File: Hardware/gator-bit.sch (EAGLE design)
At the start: 89 parts, among them J1 GATOR, J10 GATOR, J11 GATOR, J12 GATOR, J13 GATOR, J14 GATOR, J15 GATOR, J16 GATOR, J17 GATOR, J18 GATOR, J2 GATOR, J3 GATOR, J4 GATOR, J6 GATOR, J7 GATOR, J8 GATOR, J9 GATOR, U1 TPS63070, U2 micro:bit, U3 MIC52053.0V, U4 ADJ REG 1.5A

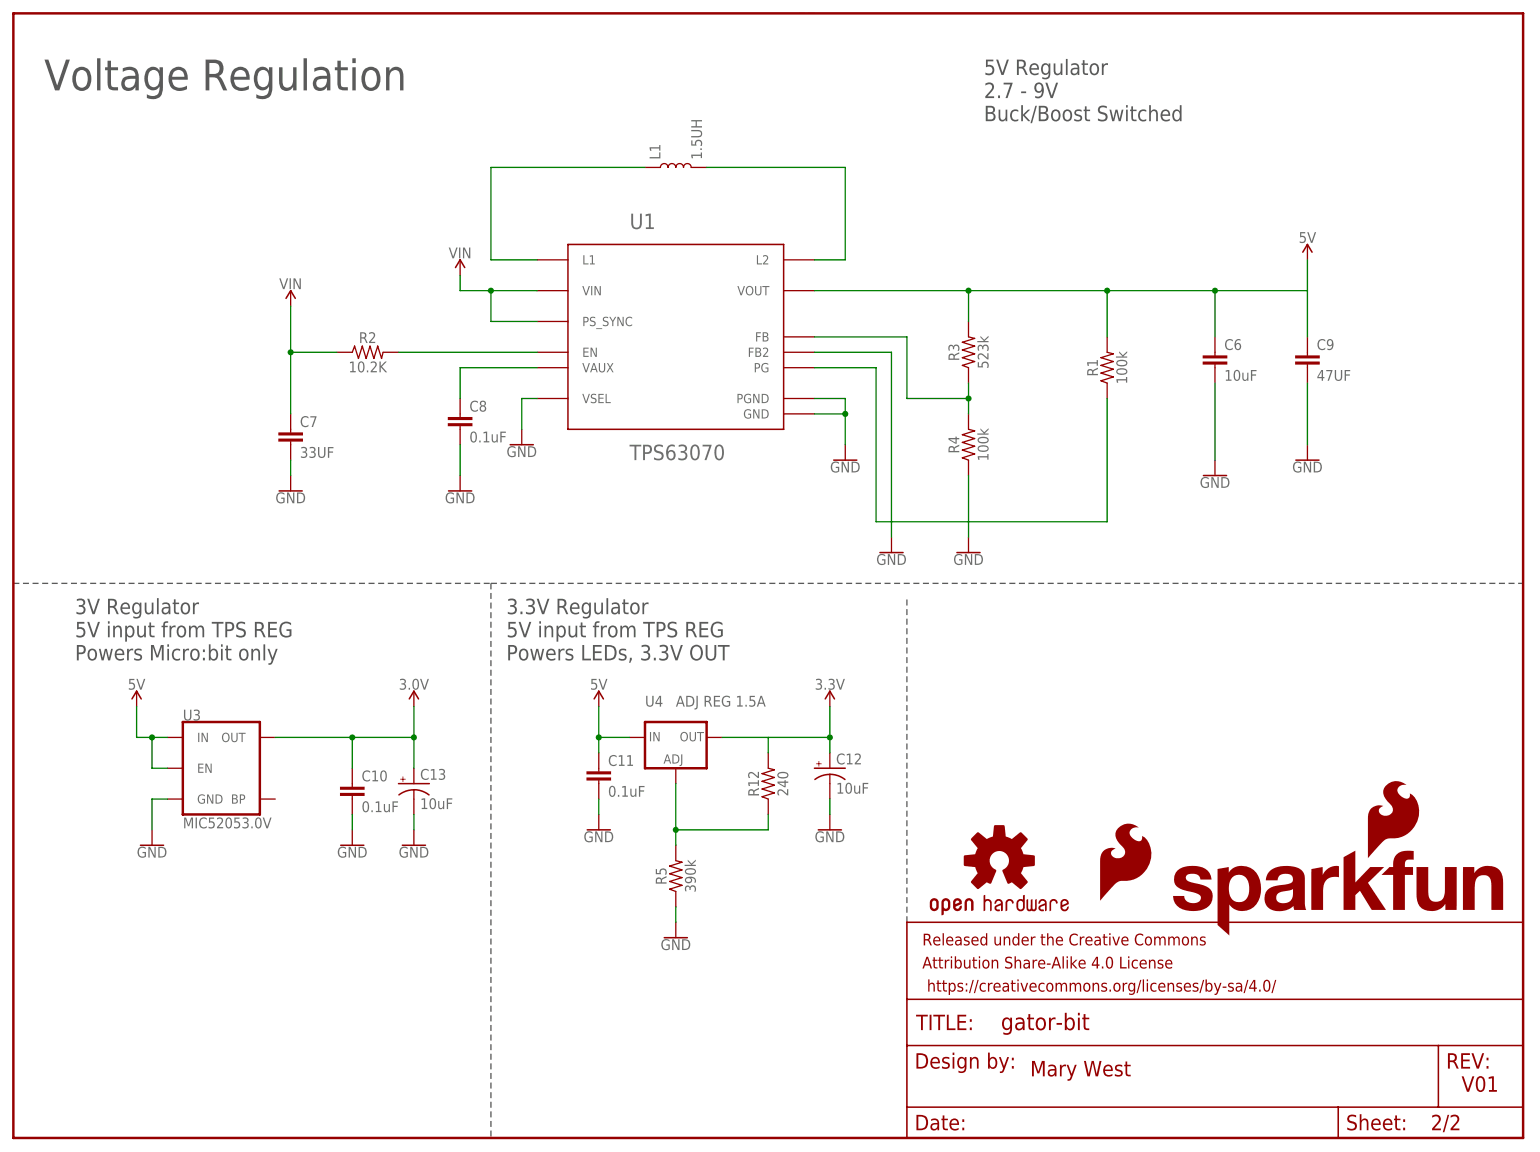
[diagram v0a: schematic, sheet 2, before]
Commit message: -Updated protection diodes -added a power path to be powered from the micro:bit -added master switch -added status LEDs
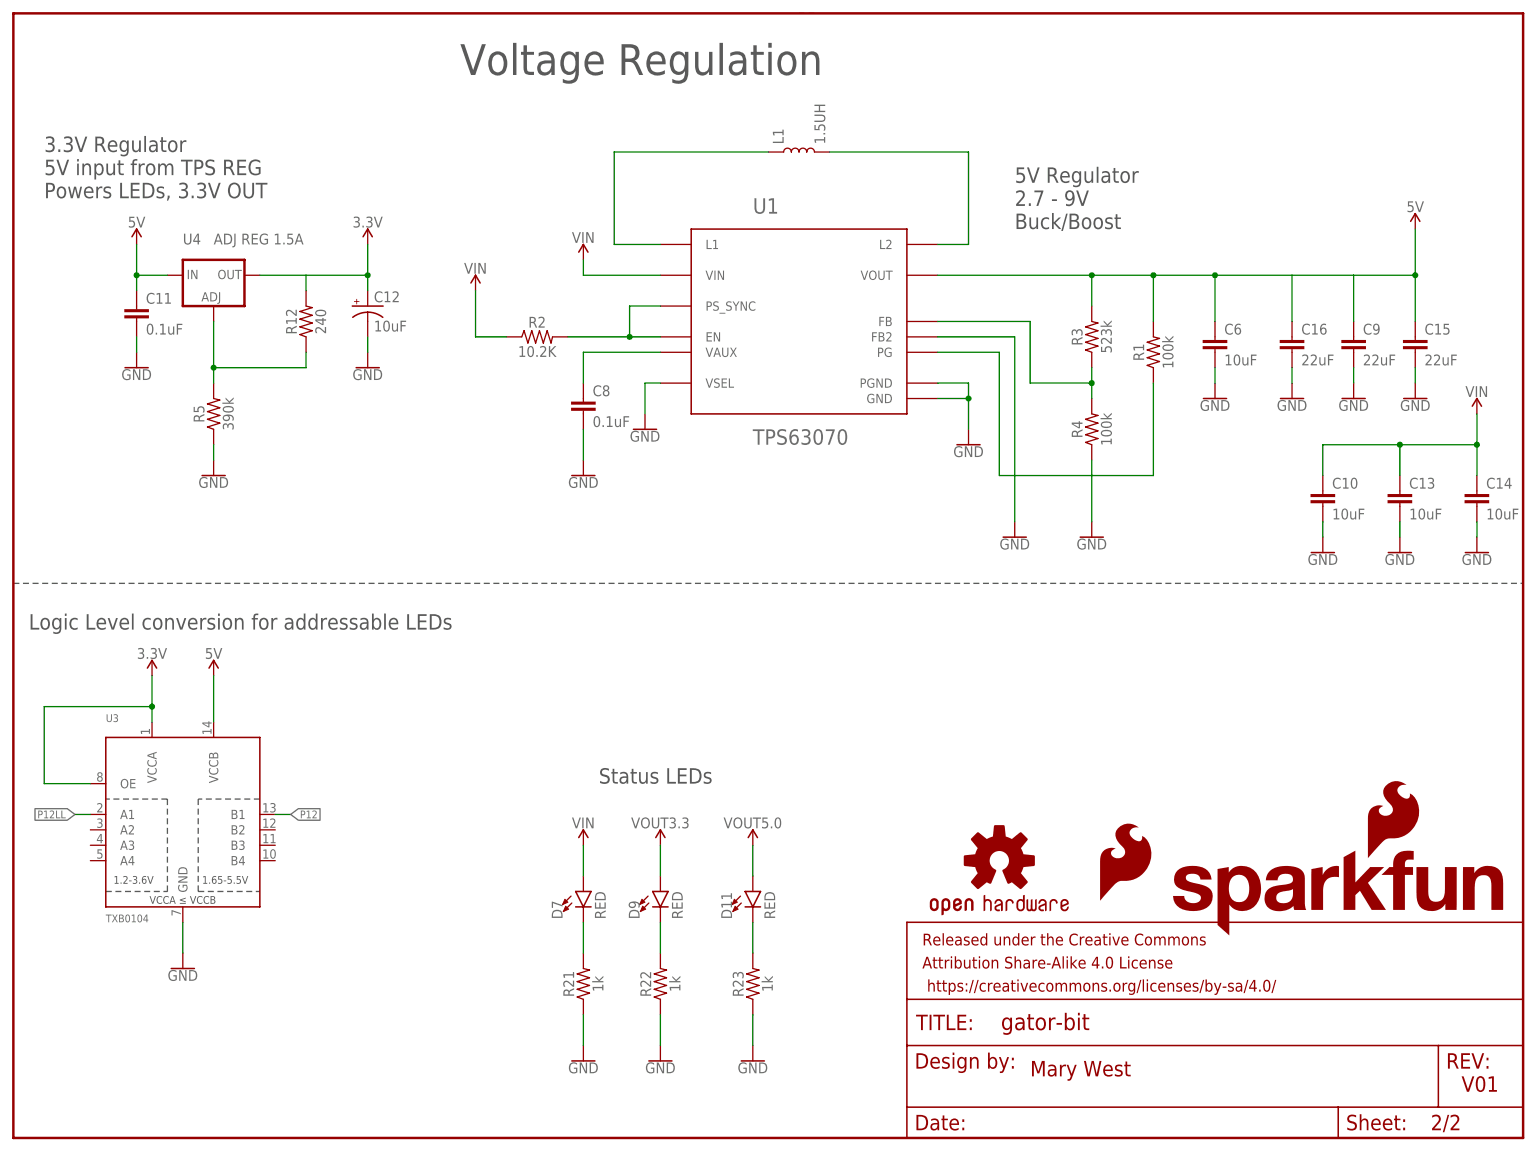
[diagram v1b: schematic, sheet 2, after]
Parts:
- removed C7: 33UF, SparkFun-Capacitors:33UF20%-6.3V-0805
- removed D14, D16, D18, D20: 3.3V, SparkFun-DiscreteSemi:DIODE-ZENER-MM3Z3V3T1G
- added C14: 10uF, SparkFun-Capacitors:10UF-0603-6.3V-20%
- added C15, C16: 22uF, SparkFun-Capacitors:22UF-0805-6.3V-20%
- added R21, R22, R23: 1k, SparkFun-Resistors:1KOHM-0603-1/10W-1%
- added S4: (no value), SparkFun-Switches:SWITCH-SPDT-SMD-AYZ0202
- C10: value 0.1uF -> 10uF; device SparkFun-Capacitors:0.1UF-0603-25V-(+80/-20%) -> SparkFun-Capacitors:10UF-0805-10V-10%
- C13: device SparkFun-Capacitors:10UF-POLAR-EIA3216-16V-10%(TANT) -> SparkFun-Capacitors:10UF-0805-10V-10%
- C9: value 47UF -> 22uF; device SparkFun-Capacitors:47UF20%-6.3V-0805 -> SparkFun-Capacitors:22UF-0805-6.3V-20%
- D10, D12, D13, D15, D17, D19, D8: value 3.3V -> 3.8V; device SparkFun-DiscreteSemi:DIODE-ZENER-MM3Z3V3T1G -> PDZVTR36BCT:PDZVTR3.6B
- D11, D7, D9: value 3.3V -> RED; device SparkFun-DiscreteSemi:DIODE-ZENER-MM3Z3V3T1G -> SparkFun-LED:LED-RED0603
- U3: value MIC52053.0V -> TXB0104; device SparkFun-IC-Power:V_REG_MIC52053.0V -> SparkFun-IC-Comms:TXB0104PWR
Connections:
- removed net 3.0V: C10.1, C13.+, D11.C, D14.C, D16.C, D18.C, D20.C, D7.C, D9.C, U2.3.3V, U3.OUT
- new net N$23: D9.C, R22.2
- new net N$24: D11.C, R23.2
- new net N$9: D7.C, R21.2
- new net P12LL: U2.P12, U3.A1
- new net VSUPPLY: S2.P, S4.P
- net 3.3V: now also U2.3.3V, U3.OE, U3.VCCA; no longer C1.2, C2.2, C3.2, C4.2, C5.2, D1.VDD, D2.VDD, D3.VDD, D4.VDD, D5.VDD
- net 5V: now also C1.2, C15.1, C16.1, C2.2, C3.2, C4.2, C5.2, D1.VDD, D2.VDD, D3.VDD, D4.VDD, D5.VDD, U3.VCCB; no longer U3.EN, U3.IN
- net GND: now also C13.2, C14.2, C15.2, C16.2, R21.1, R22.1, R23.1; no longer C13.-, C7.2
- net N$13: now also U1.PS_SYNC
- net P12: now also U3.B1; no longer U2.P12
- net PP0: no longer D14.A
- net PP1: no longer D16.A
- net PP11: no longer D11.A
- net PP16: no longer D7.A
- net PP2: no longer D18.A
- net PP5: no longer D20.A
- net PP8: no longer D9.A
- net VIN: now also C10.1, C13.1, C14.1, D7.A, S4.S; no longer C7.1, S2.P, U1.PS_SYNC
- net VOUT3.3: now also D9.A
- net VOUT5.0: now also D11.A
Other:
- note added: "5V Regulator 2.7 - 9V Buck/Boost"
- note added: "Logic Level conversion for addressable LEDs"
- note added: "Master Switch"
- note added: "Status LEDs"
- note removed: "3V Regulator 5V input from TPS REG Powers Micro:bit only"
- note removed: "5V Regulator 2.7 - 9V Buck/Boost Switched"
- moved on the sheet: C10, C11, C12, C6, C8, C9, D10, D12, D13, D17, D6, D8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

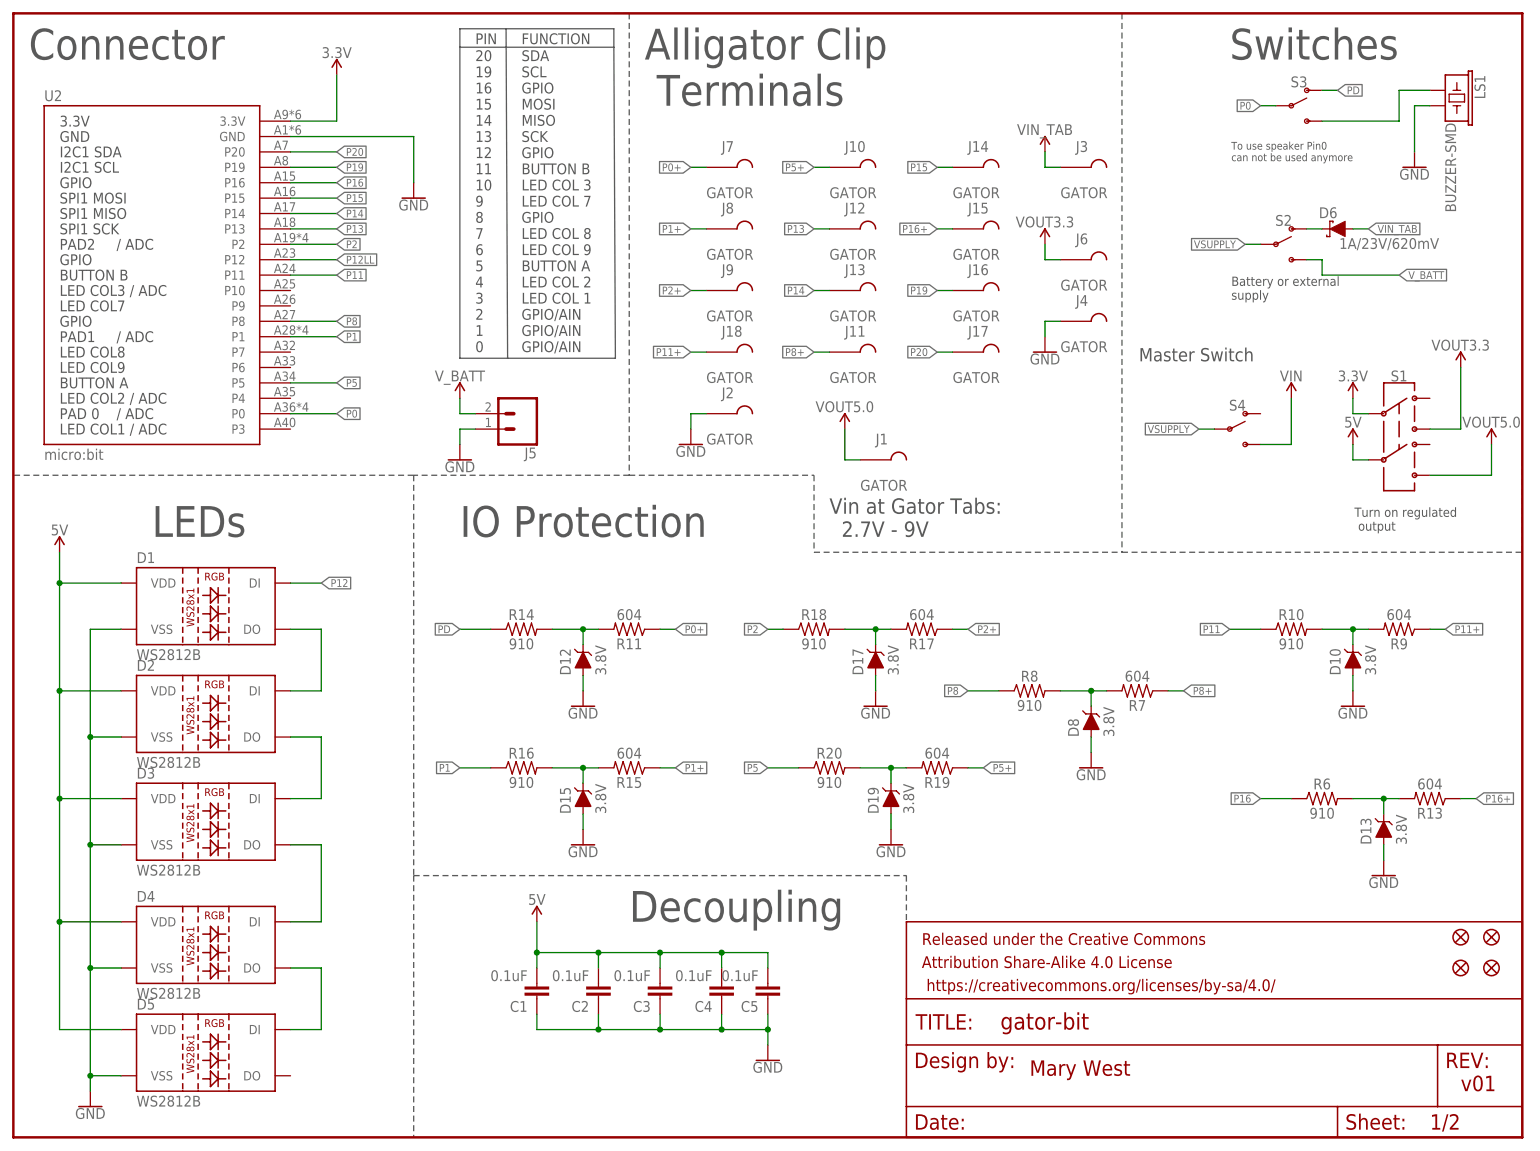
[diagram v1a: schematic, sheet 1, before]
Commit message: -Added Fuse to 3.3V input on the m:b -added silk to show users the sequence of switches -added option to choose powering from m:b (USB) or from an external power supply.
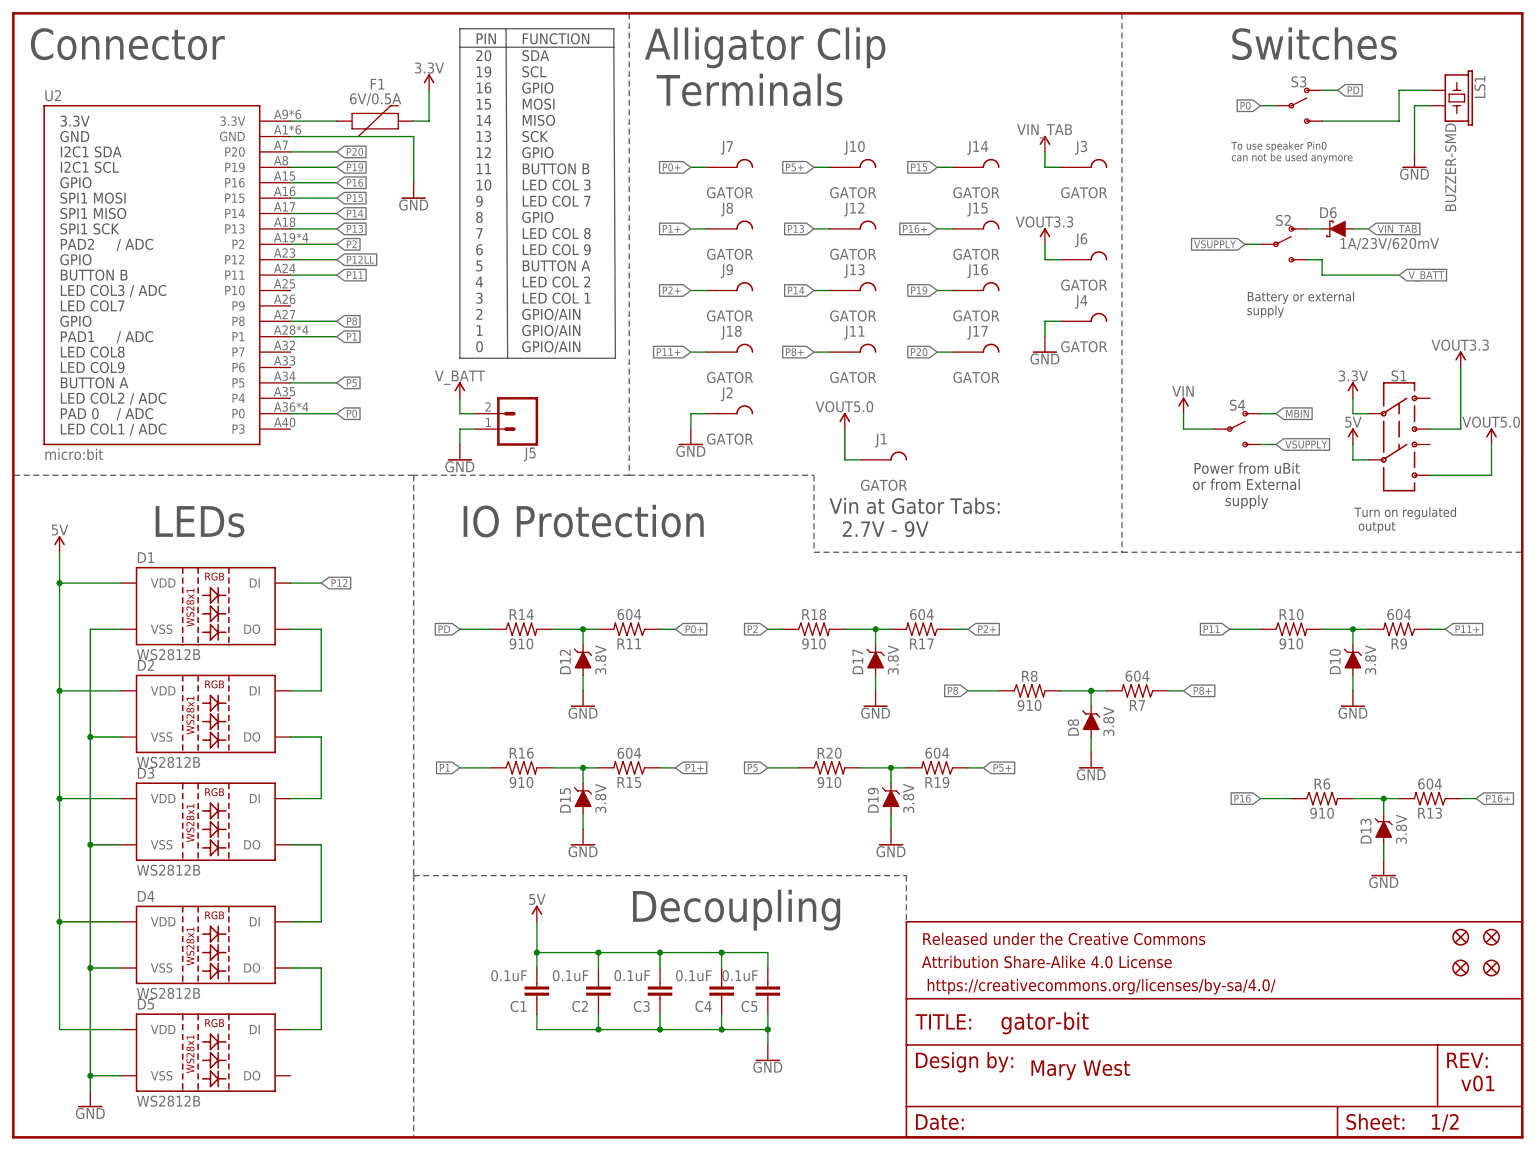
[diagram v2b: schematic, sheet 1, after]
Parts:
- added F1: 6V/0.5A, SparkFun-Fuses:PPTC_HALF-AMP
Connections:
- new net MBIN: F1.1, S4.O, U2.3.3V
- net 3.3V: now also F1.2; no longer U2.3.3V
- net VIN: now also S4.P; no longer S4.S
- net VSUPPLY: now also S4.S; no longer S4.P
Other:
- note added: "Power from uBit or from External supply"
- note removed: "Master Switch"
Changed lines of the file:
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@@
 <part name="LOGO6" library="SparkFun-Aesthetics" deviceset="OSHW-LOGO" device="L"/>
 <part name="SUPPLY1" library="SparkFun-PowerSymbols" deviceset="5V" device=""/>
-<part name="SUPPLY3" library="SparkFun-PowerSymbols" deviceset="3.3V" device=""/>
 <part name="C10" library="SparkFun-Capacitors" deviceset="10UF" device="-0805-10V-10%" value="10uF"/>
 <part name="C13" library="SparkFun-Capacitors" deviceset="10UF" device="-0805-10V-10%" value="10uF"/>
@@
 <part name="SUPPLY13" library="SparkFun-PowerSymbols" deviceset="VOUT" device="" value="VOUT3.3"/>
 <part name="SUPPLY14" library="SparkFun-PowerSymbols" deviceset="5V" device="" value="VOUT5.0"/>
+<part name="F1" library="SparkFun-Fuses" deviceset="PPTC" device="_HALF-AMP" value="6V/0.5A"/>
+<part name="SUPPLY3" library="SparkFun-PowerSymbols" deviceset="3.3V" device=""/>
 </parts>
 <sheets>
@@
 <text x="200.914" y="161.036" size="1.27" layer="97" font="vector">To use speaker Pin0
 can not be used anymore</text>
-<text x="200.914" y="138.176" size="1.524" layer="97" font="vector">Battery or external
+<text x="203.454" y="135.636" size="1.524" layer="97" font="vector">Battery or external
 supply</text>
 <text x="221.234" y="100.076" size="1.524" layer="97" font="vector">Turn on regulated
@@
 <wire x1="132.08" y1="109.22" x2="132.08" y2="96.52" width="0.1524" layer="97" style="shortdash"/>
 <wire x1="132.08" y1="96.52" x2="182.88" y2="96.52" width="0.1524" layer="97" style="shortdash"/>
-<text x="185.674" y="128.016" size="2.1844" layer="97" font="vector">Master Switch </text>
+<text x="203.454" y="107.696" size="1.778" layer="97" font="vector" align="center">Power from uBit
+or from External
+supply</text>
 </plain>
 <instances>
@@
 </instance>
 <instance part="SUPPLY1" gate="G$1" x="7.62" y="96.52"/>
-<instance part="SUPPLY3" gate="G$1" x="53.34" y="175.26"/>
 <instance part="SUPPLY6" gate="G$1" x="86.36" y="35.56"/>
 <instance part="S4" gate="1" x="200.66" y="116.84"/>
-<instance part="SUPPLY9" gate="G$1" x="210.82" y="121.92"/>
+<instance part="SUPPLY9" gate="G$1" x="193.04" y="119.38"/>
+<instance part="F1" gate="G$1" x="58.42" y="167.64" smashed="yes">
+<attribute name="NAME" x="60.071" y="172.847" size="1.778" layer="95" font="vector" align="bottom-center"/>
+<attribute name="VALUE" x="59.69" y="172.212" size="1.778" layer="96" font="vector" align="top-center"/>
+</instance>
+<instance part="SUPPLY3" gate="G$1" x="68.58" y="172.72"/>
 </instances>
 <busses>
@@
 </segment>
 <segment>
-<pinref part="U2" gate="G$1" pin="3.3V"/>
-<wire x1="45.72" y1="167.64" x2="53.34" y2="167.64" width="0.1524" layer="91"/>
-<wire x1="53.34" y1="167.64" x2="53.34" y2="175.26" width="0.1524" layer="91"/>
+<pinref part="F1" gate="G$1" pin="2"/>
+<wire x1="66.04" y1="167.64" x2="68.58" y2="167.64" width="0.1524" layer="91"/>
+<wire x1="68.58" y1="167.64" x2="68.58" y2="172.72" width="0.1524" layer="91"/>
 <pinref part="SUPPLY3" gate="G$1" pin="3.3V"/>
 </segment>
@@
 </segment>
 <segment>
+<pinref part="S4" gate="1" pin="S"/>
+<wire x1="205.74" y1="114.3" x2="208.28" y2="114.3" width="0.1524" layer="91"/>
+<label x="208.28" y="114.3" size="1.27" layer="95" xref="yes"/>
+</segment>
+</net>
+<net name="VIN" class="0">
+<segment>
 <pinref part="S4" gate="1" pin="P"/>
-<wire x1="198.12" y1="116.84" x2="195.58" y2="116.84" width="0.1524" layer="91"/>
-<label x="195.58" y="116.84" size="1.27" layer="95" rot="R180" xref="yes"/>
-</segment>
-</net>
-<net name="VIN" class="0">
-<segment>
-<wire x1="210.82" y1="114.3" x2="210.82" y2="121.92" width="0.1524" layer="91"/>
+<wire x1="198.12" y1="116.84" x2="193.04" y2="116.84" width="0.1524" layer="91"/>
+<wire x1="193.04" y1="116.84" x2="193.04" y2="119.38" width="0.1524" layer="91"/>
 <pinref part="SUPPLY9" gate="G$1" pin="VIN"/>
-<pinref part="S4" gate="1" pin="S"/>
-<wire x1="205.74" y1="114.3" x2="210.82" y2="114.3" width="0.1524" layer="91"/>
-</segment>
-</net>
+</segment>
+</net>
+<net name="MBIN" class="0">
+<segment>
+<pinref part="U2" gate="G$1" pin="3.3V"/>
+<wire x1="45.72" y1="167.64" x2="53.34" y2="167.64" width="0.1524" layer="91"/>
+<pinref part="F1" gate="G$1" pin="1"/>
+</segment>
+<segment>
+<pinref part="S4" gate="1" pin="O"/>
+<wire x1="205.74" y1="119.38" x2="208.28" y2="119.38" width="0.1524" layer="91"/>
+<label x="208.28" y="119.38" size="1.27" layer="95" xref="yes"/>
+</segment>
+</net>

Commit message: v02, silk
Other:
- note added: "v02"
- note removed: "v01"
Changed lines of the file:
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@@
 <sheet>
 <plain>
-<text x="238.76" y="7.62" size="2.54" layer="94">v01</text>
+<text x="238.76" y="7.62" size="2.54" layer="94">v02</text>
 <text x="2.54" y="177.8" size="5.08" layer="97" font="vector">Connector</text>
 <text x="76.2" y="129.54" size="1.778" layer="97">20
